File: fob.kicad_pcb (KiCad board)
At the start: 2 copper layers, 53 x 53 mm, 10 parts, among them P1 SW DBG, P2 SOIC16-ZIF

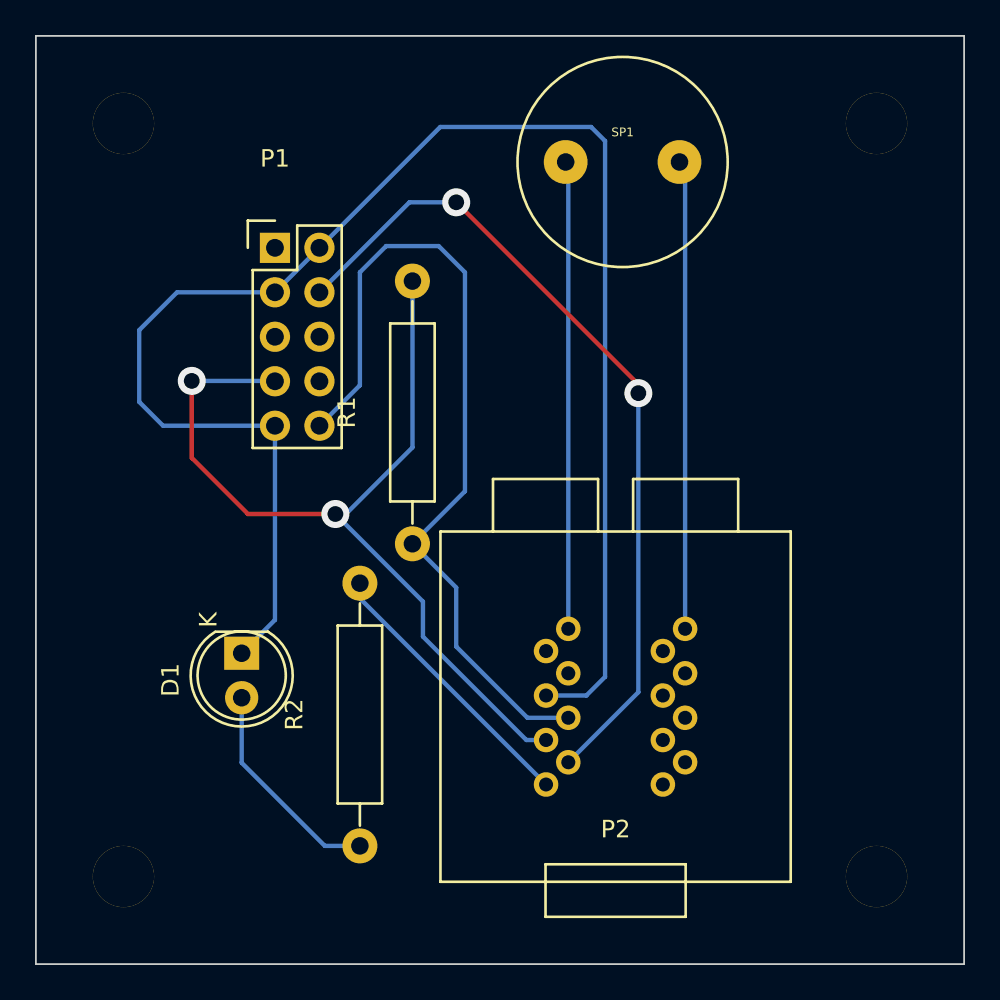
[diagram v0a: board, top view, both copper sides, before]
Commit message: finished final cut version that is do-or-die; parts fit
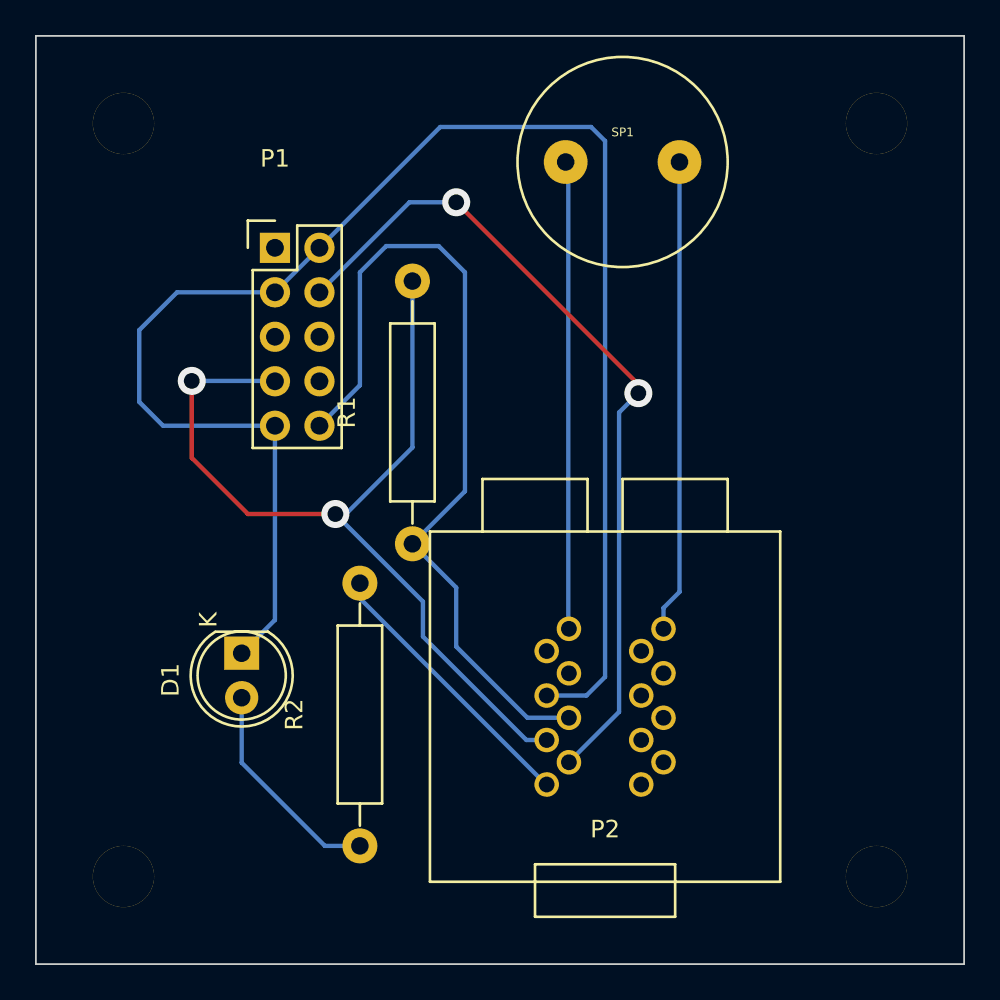
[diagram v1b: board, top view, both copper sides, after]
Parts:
- moved P2 0.60 mm to (139.5, 113.3)
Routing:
- net Net-(P2-Pad16): track 26.8 -> 27.5 mm
